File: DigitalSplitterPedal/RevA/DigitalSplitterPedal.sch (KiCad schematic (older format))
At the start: 10 parts, among them J1 MonoJack2Switch, J2 Barrel_Jack, J3 MonoJack2Switch, J4 MonoJack2Switch, J5 MonoJack2Switch, J6 MonoJack2Switch

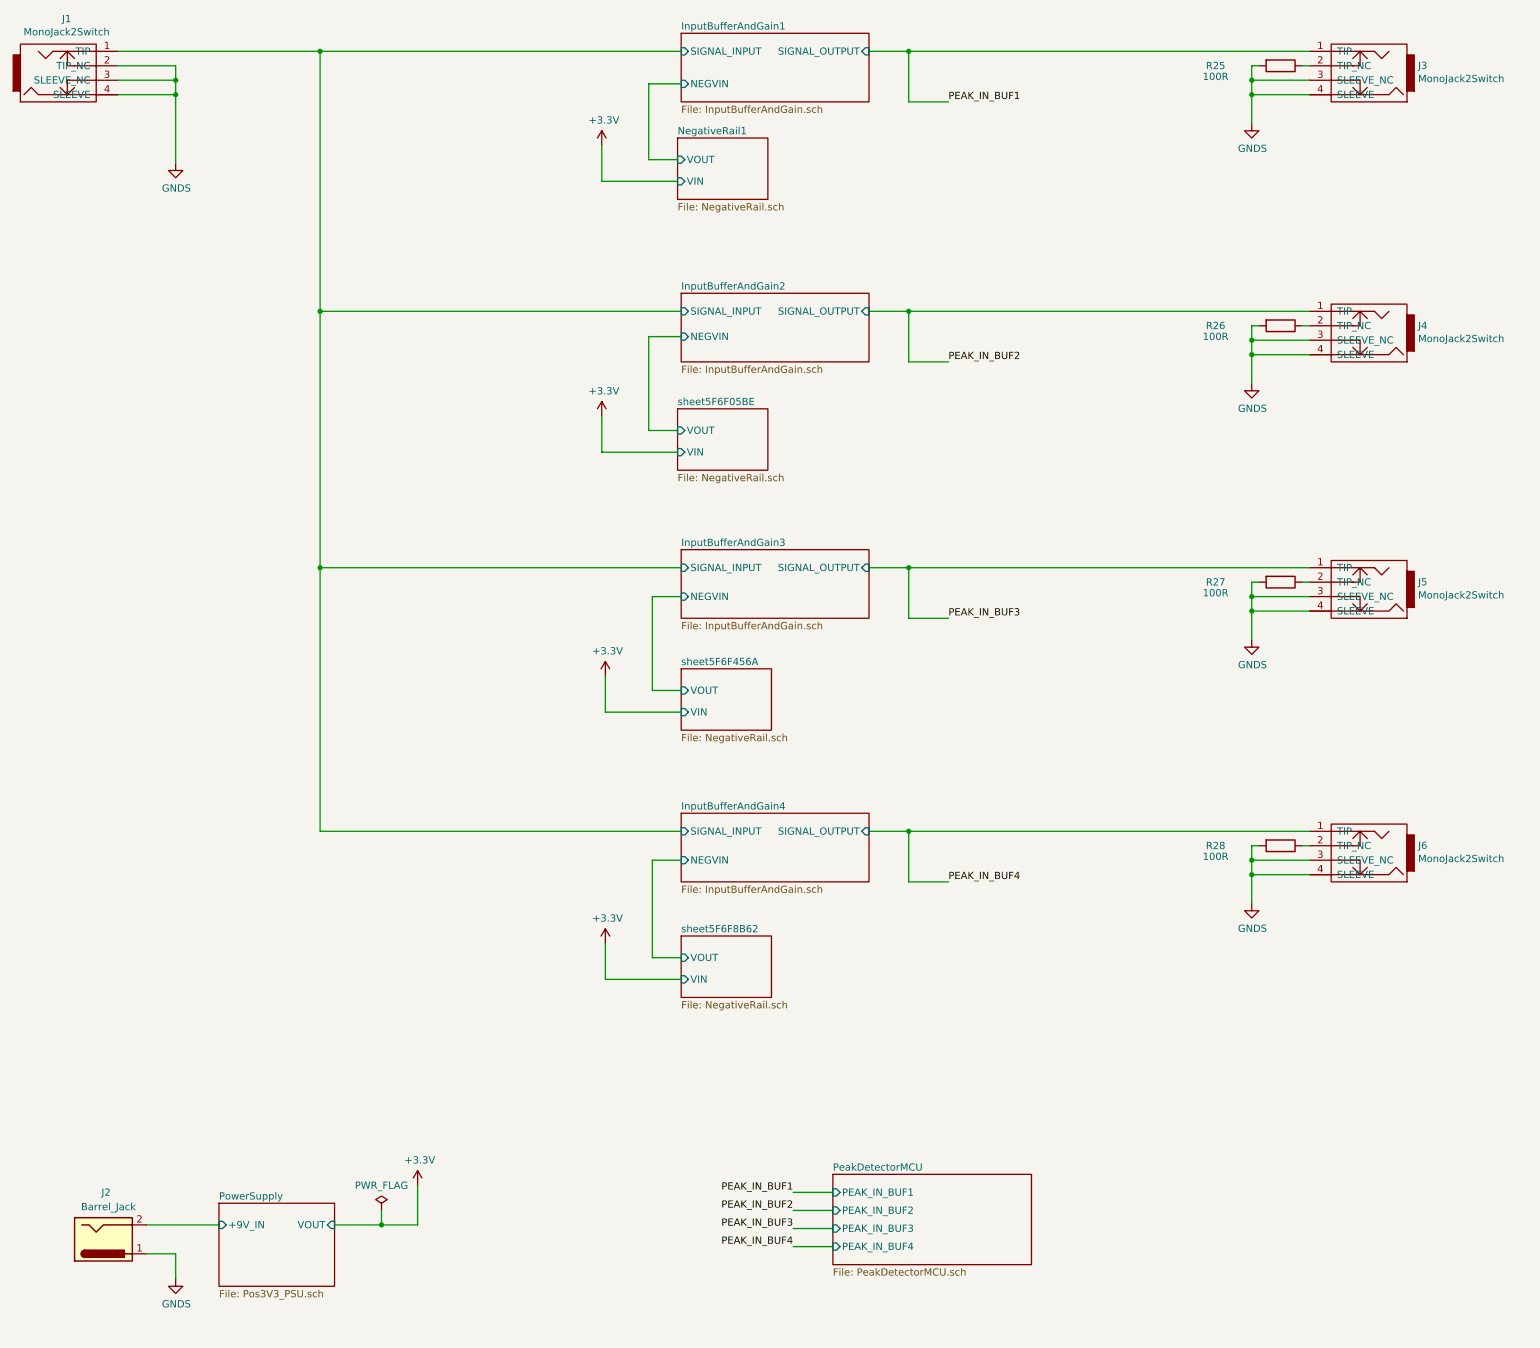
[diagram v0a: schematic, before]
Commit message: updated hw
- add testpoints
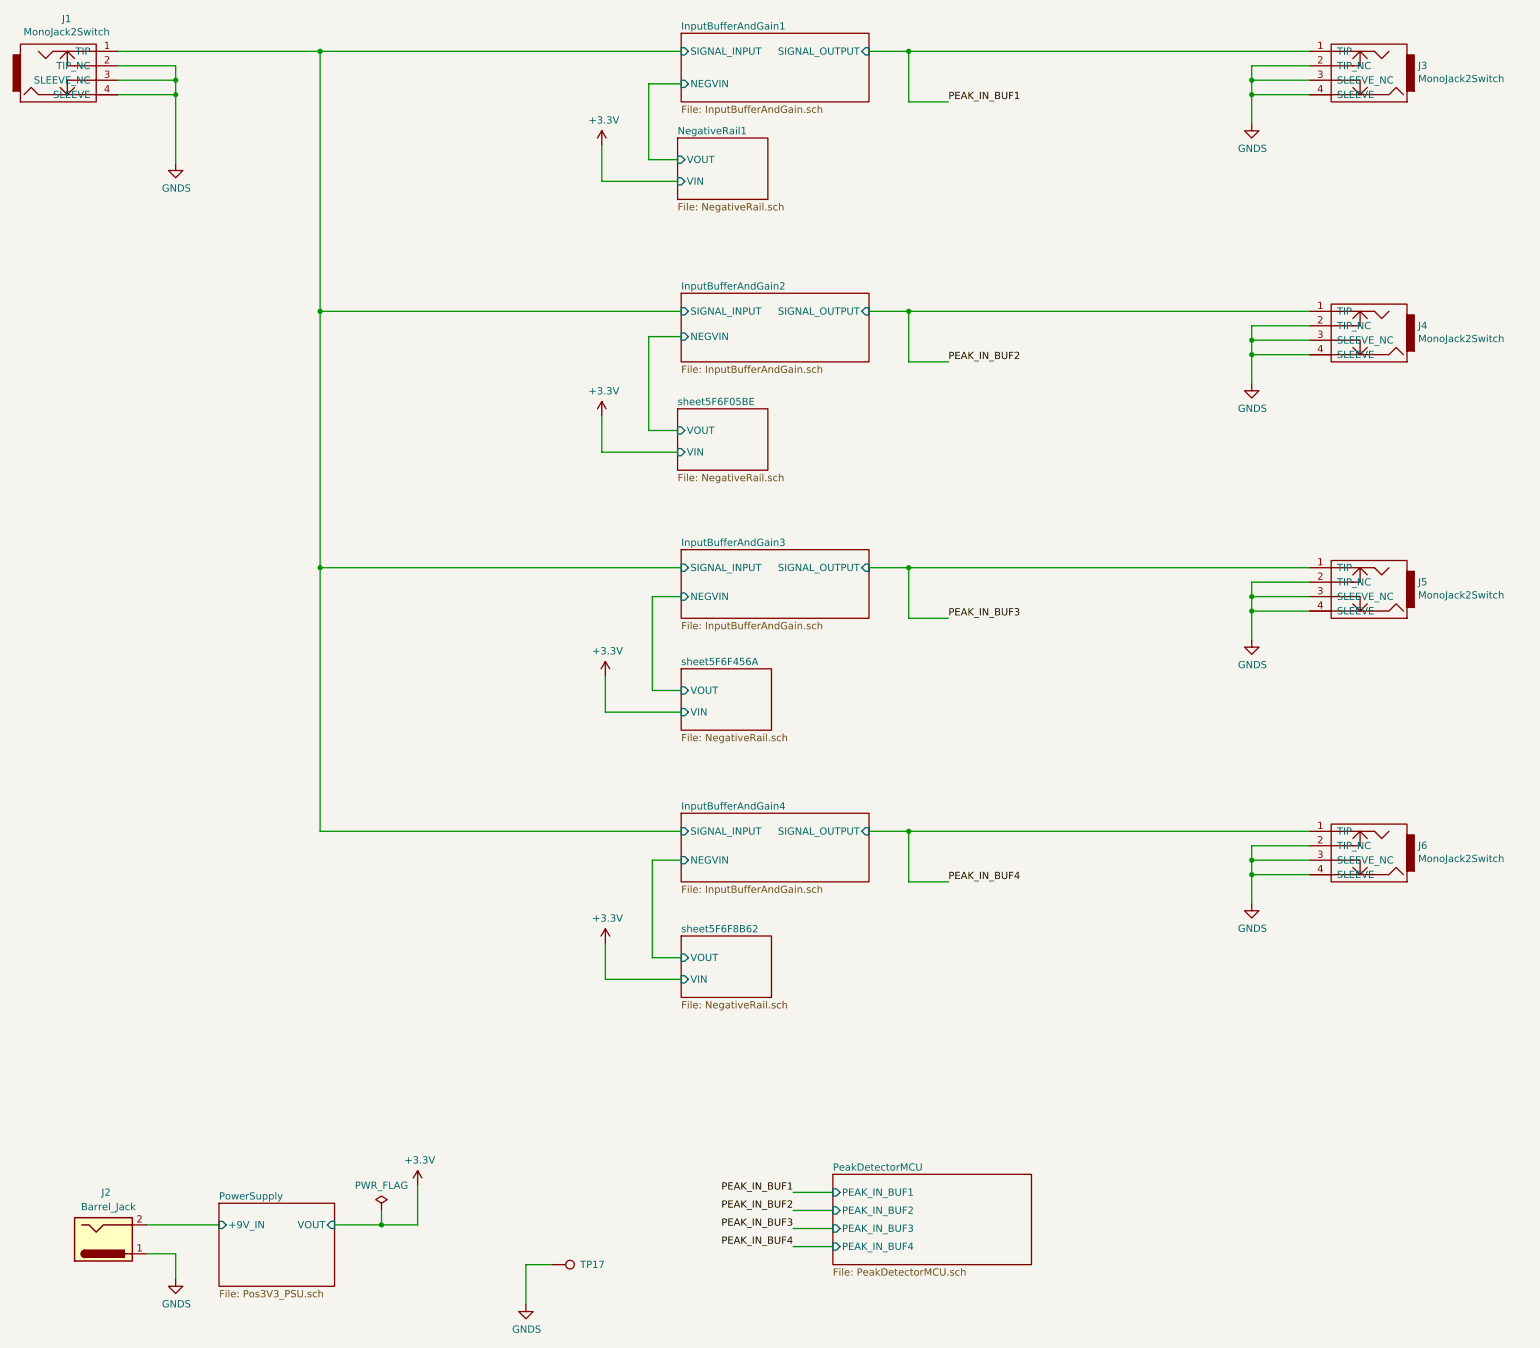
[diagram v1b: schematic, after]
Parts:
- removed R25, R26, R27, R28: 100R, Capacitor_SMD:C_0805_2012Metric_Pad1.15x1.40mm_HandSolder, symbol Device:R
- added TP17: TestPoint, TestPoint:TestPoint_Pad_D1.0mm, symbol Connector:TestPoint
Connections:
- net GNDS: now also J3.2 (TIP_NC), J4.2 (TIP_NC), J5.2 (TIP_NC), J6.2 (TIP_NC), TP17.1
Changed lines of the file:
@@
 	10900 7100 10900 7200
-Wire Wire Line
-	11300 7100 11250 7100
 Wire Wire Line
 	10900 5475 10900 5675
@@
 	10900 5275 10900 5375
 Wire Wire Line
-	11300 5275 11250 5275
-Wire Wire Line
 	10900 3700 10900 3900
 Connection ~ 10900 3700
@@
 	10900 3500 10900 3600
 Wire Wire Line
-	11300 3500 11250 3500
-Wire Wire Line
 	10900 1900 10900 2100
 Connection ~ 10900 1900
@@
 Wire Wire Line
 	10900 1700 10900 1800
-Wire Wire Line
-	11300 1700 11250 1700
 Wire Wire Line
 	3450 1900 3450 2375
@@
 Wire Wire Line
 	8525 7000 11300 7000
-$Comp
-L Device:R R25
-U 1 1 5F62BA16
-P 11100 1700
-F 0 "R25" V 11100 1250 50  0000 C CNN
-F 1 "100R" V 11175 1250 50  0000 C CNN
-F 2 "Capacitor_SMD:C_0805_2012Metric_Pad1.15x1.40mm_HandSolder" V 11030 1700 50  0001 C CNN
-F 3 "~" H 11100 1700 50  0001 C CNN
-	1    11100 1700
-	0    1    1    0
-$EndComp
-Wire Wire Line
-	10950 1700 10900 1700
-$Comp
-L Device:R R26
-U 1 1 5F62C4AF
-P 11100 3500
-F 0 "R26" V 11100 3050 50  0000 C CNN
-F 1 "100R" V 11175 3050 50  0000 C CNN
-F 2 "Capacitor_SMD:C_0805_2012Metric_Pad1.15x1.40mm_HandSolder" V 11030 3500 50  0001 C CNN
-F 3 "~" H 11100 3500 50  0001 C CNN
-	1    11100 3500
-	0    1    1    0
-$EndComp
-Wire Wire Line
-	10950 3500 10900 3500
-$Comp
-L Device:R R27
-U 1 1 5F62CF86
-P 11100 5275
-F 0 "R27" V 11100 4825 50  0000 C CNN
-F 1 "100R" V 11175 4825 50  0000 C CNN
-F 2 "Capacitor_SMD:C_0805_2012Metric_Pad1.15x1.40mm_HandSolder" V 11030 5275 50  0001 C CNN
-F 3 "~" H 11100 5275 50  0001 C CNN
-	1    11100 5275
-	0    1    1    0
-$EndComp
-Wire Wire Line
-	10950 5275 10900 5275
-$Comp
-L Device:R R28
-U 1 1 5F62D6CF
-P 11100 7100
-F 0 "R28" V 11100 6650 50  0000 C CNN
-F 1 "100R" V 11175 6650 50  0000 C CNN
-F 2 "Capacitor_SMD:C_0805_2012Metric_Pad1.15x1.40mm_HandSolder" V 11030 7100 50  0001 C CNN
-F 3 "~" H 11100 7100 50  0001 C CNN
-	1    11100 7100
-	0    1    1    0
-$EndComp
-Wire Wire Line
-	10950 7100 10900 7100
 $Sheet
 S 6925 2200 625  425
@@
 F3 "VOUT" I R 4550 9725 50
 $EndSheet
+Wire Wire Line
+	10900 7100 11300 7100
+Wire Wire Line
+	10900 5275 11300 5275
+Wire Wire Line
+	10900 3500 11300 3500
+Wire Wire Line
+	10900 1700 11300 1700
+$Comp
+L Connector:TestPoint TP?
+U 1 1 5F719EBF
+P 6050 10000
+AR Path="/5F6CB11D/5F719EBF" Ref="TP?"  Part="1"
+AR Path="/5F6F05C2/5F719EBF" Ref="TP?"  Part="1"
+AR Path="/5F6F456E/5F719EBF" Ref="TP?"  Part="1"
+AR Path="/5F6F8B66/5F719EBF" Ref="TP?"  Part="1"
+AR Path="/5F6CB23D/5F719EBF" Ref="TP?"  Part="1"
+AR Path="/5F719EBF" Ref="TP17"  Part="1"
+F 0 "TP17" V 6050 10200 50  0000 L CNN
+F 1 "TestPoint" V 5825 9950 50  0001 L CNN
+F 2 "TestPoint:TestPoint_Pad_D1.0mm" H 6250 10000 50  0001 C CNN
+F 3 "~" H 6250 10000 50  0001 C CNN
+	1    6050 10000
+	0    1    1    0
+$EndComp
+Wire Wire Line
+	6050 10000 5875 10000
+Wire Wire Line
+	5875 10000 5875 10275
+$Comp
+L power:GNDS #PWR026
+U 1 1 5F71E908
+P 5875 10275
+F 0 "#PWR026" H 5875 10025 50  0001 C CNN
+F 1 "GNDS" H 5880 10102 50  0000 C CNN
+F 2 "" H 5875 10275 50  0001 C CNN
+F 3 "" H 5875 10275 50  0001 C CNN
+	1    5875 10275
+	1    0    0    -1
+$EndComp
 $EndSCHEMATC
